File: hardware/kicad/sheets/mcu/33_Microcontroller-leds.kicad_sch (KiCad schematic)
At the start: 17 parts, among them U200 WS2815F, U201 WS2815F, U202 WS2815F, U203 WS2815F, U204 74AHCT1G125GW,125-JSM, U205 WS2815F, U206 74AHCT1G125GW,125-JSM, U207 ZX-VH3.96-4PWZ

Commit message: reorganized
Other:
- title: Microcontroller-leds -> Status LEDs
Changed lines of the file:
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@@
 	(paper "User" 297 210)
 	(title_block
-		(title "Microcontroller-leds")
+		(title "Status LEDs")
 		(date "2026-02-16")
 	)

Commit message: before final cleanup
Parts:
- renumbered C296 to C49, C295 to C50, C294 to C51, C299 to C52, C298 to C53, C297 to C54, H5 to H3, R524 to R111, R525 to R112, U204 to U27, U205 to U28, U206 to U29, U203 to U30, U202 to U31, U207 to U32, U201 to U33, U200 to U34

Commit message: pre kicad footprints
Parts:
- H3: footprint 5v rail sm-easyedapro:HDR-TH_2P-P2.54-V-M -> Connector_PinHeader_2.54mm:PinHeader_1x02_P2.54mm_Vertical
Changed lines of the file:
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@@
 			)
 		)
-		(property "Footprint" "5v rail sm-easyedapro:HDR-TH_2P-P2.54-V-M"
+		(property "Footprint" "Connector_PinHeader_2.54mm:PinHeader_1x02_P2.54mm_Vertical"
 			(at 181.61 120.65 0)
 			(effects

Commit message: imrpved footprints
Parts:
- U32: footprint 5v rail sm-easyedapro:CONN-TH_ZX-VH3.96-4PWZ -> Connector_JST:JST_VH_B4P-VH_1x04_P3.96mm_Vertical
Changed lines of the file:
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@@
 			)
 		)
-		(property "Footprint" "5v rail sm-easyedapro:CONN-TH_ZX-VH3.96-4PWZ"
+		(property "Footprint" "Connector_JST:JST_VH_B4P-VH_1x04_P3.96mm_Vertical"
 			(at 196.85 133.35 0)
 			(effects

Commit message: added better footprints and steps
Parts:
- removed U32: ZX-VH3.96-4PWZ, Connector_JST:JST_VH_B4P-VH_1x04_P3.96mm_Vertical, symbol 5v rail sm-easyedapro:ZX-VH3.96-4PWZ
- added U69: VH3_96-4P_ZZ, JLCImport:VH3_96-4P_ZZ, symbol JLCImport:VH3_96-4P_ZZ
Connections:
- net +12V: now also U69.1
- net GND: now also U69.4
- net at H3.2, R112.2: now also U69.2
- net at H3.1: now also U69.3
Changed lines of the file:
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@@
-	)
-	(symbol
-		(lib_id "5v rail sm-easyedapro:ZX-VH3.96-4PWZ")
-		(at 196.85 133.35 0)
-		(unit 1)
-		(exclude_from_sim no)
-		(in_bom yes)
-		(on_board yes)
-		(dnp no)
-		(property "Reference" "U32"
-			(at 194.31 127 0)
-			(effects
-				(font
-					(size 1.27 1.27)
-				)
-				(justify left bottom)
-			)
-		)
-		(property "Value" "ZX-VH3.96-4PWZ"
-			(at 194.31 142.24 0)
-			(effects
-				(font
-					(size 1.27 1.27)
-				)
-				(justify left bottom)
-			)
-		)
-		(property "Footprint" "Connector_JST:JST_VH_B4P-VH_1x04_P3.96mm_Vertical"
-			(at 196.85 133.35 0)
-			(effects
-				(font
-					(size 1.27 1.27)
-				)
-				(hide yes)
-			)
-		)
-		(property "Datasheet" "https://item.szlcsc.com/datasheet/ZX-VH3.96-4PWZ/8427586.html"
-			(at 196.85 133.35 0)
-			(effects
-				(font
-					(size 1.27 1.27)
-				)
-				(hide yes)
-			)
-		)
-		(property "Description" "Pins Structure:1x4P Pitch:3.96mm Mounting Type:Right Angle Reference Series:VH Number of Pins:4P Number of Rows:1 Number of PINs Per Row:4 Row Spacing:- Current Rating:3A Contact Material:Brass Contact Plating:Tin Operating Temperature:-25°C~+85°C Operating"
-			(at 196.85 133.35 0)
-			(effects
-				(font
-					(size 1.27 1.27)
-				)
-				(hide yes)
-			)
-		)
-		(property "Manufacturer Part" "ZX-VH3.96-4PWZ"
-			(at 196.85 133.35 0)
-			(effects
-				(font
-					(size 1.27 1.27)
-				)
-				(hide yes)
-			)
-		)
-		(property "Manufacturer" "Megastar(兆星)"
-			(at 196.85 133.35 0)
-			(effects
-				(font
-					(size 1.27 1.27)
-				)
-				(hide yes)
-			)
-		)
-		(property "Supplier Part" "C7429669"
-			(at 196.85 133.35 0)
-			(effects
-				(font
-					(size 1.27 1.27)
-				)
-				(hide yes)
-			)
-		)
-		(property "Supplier" "LCSC"
-			(at 196.85 133.35 0)
-			(effects
-				(font
-					(size 1.27 1.27)
-				)
-				(hide yes)
-			)
-		)
-		(property "LCSC Part Name" "1x4P 间距:3.96mm 弯插 系列:VH"
-			(at 196.85 133.35 0)
-			(effects
-				(font
-					(size 1.27 1.27)
-				)
-				(hide yes)
-			)
-		)
-		(pin "2"
-		)
-		(pin "1"
-		)
-		(pin "3"
-		)
-		(pin "4"
-		)
-		(instances
-			(project "svea_powerboard_rev3"
-				(path "/3f85abf4-0b95-4c4a-b7e9-06f59ca1ea3d/5c2e021f-c2d4-49e2-8c36-9a64f1f12004/8d05c3b8-20a4-4a7f-9b20-01f8d5d5be46"
-					(reference "U32")
-					(unit 1)
-				)
-			)
-		)
 	)
 	(symbol
@@
 					(unit 1)
 				)
+			)
+		)
+	)
+	(symbol
+		(lib_id "JLCImport:VH3_96-4P_ZZ")
+		(at 194.31 134.62 0)
+		(unit 1)
+		(exclude_from_sim no)
+		(in_bom yes)
+		(on_board yes)
+		(dnp no)
+		(fields_autoplaced yes)
+		(property "Reference" "U69"
+			(at 200.66 132.0799 0)
+			(effects
+				(font
+					(size 1.27 1.27)
+				)
+				(justify left)
+			)
+		)
+		(property "Value" "VH3_96-4P_ZZ"
+			(at 200.66 134.6199 0)
+			(effects
+				(font
+					(size 1.27 1.27)
+				)
+				(justify left)
+			)
+		)
+		(property "Footprint" "JLCImport:VH3_96-4P_ZZ"
+			(at 194.31 134.62 0)
+			(effects
+				(font
+					(size 1.27 1.27)
+				)
+				(hide yes)
+			)
+		)
+		(property "Datasheet" "https://atta.szlcsc.com/upload/public/pdf/source/20230630/DF786FC43E612B301379FAB1A9219773.pdf"
+			(at 194.31 134.62 0)
+			(effects
+				(font
+					(size 1.27 1.27)
+				)
+				(hide yes)
+			)
+		)
+		(property "Description" ""
+			(at 194.31 134.62 0)
+			(effects
+				(font
+					(size 1.27 1.27)
+				)
+				(hide yes)
+			)
+		)
+		(property "LCSC" "C5379870"
+			(at 194.31 134.62 0)
+			(effects
+				(font
+					(size 1.27 1.27)
+				)
+				(hide yes)
+			)
+		)
+		(property "Manufacturer" "SHOU HAN(首韩)"
+			(at 194.31 134.62 0)
+			(effects
+				(font
+					(size 1.27 1.27)
+				)
+				(hide yes)
+			)
+		)
+		(property "Manufacturer Part" "VH3.96-4P ZZ"
+			(at 194.31 134.62 0)
+			(effects
+				(font
+					(size 1.27 1.27)
+				)
+				(hide yes)
+			)
+		)
+		(pin "2"
+		)
+		(pin "1"
+		)
+		(pin "4"
+		)
+		(pin "3"
+		)
+		(instances
+			(project ""
+				(path "/3f85abf4-0b95-4c4a-b7e9-06f59ca1ea3d/5c2e021f-c2d4-49e2-8c36-9a64f1f12004/8d05c3b8-20a4-4a7f-9b20-01f8d5d5be46"
+					(reference "U69")
+					(unit 1)
+				)

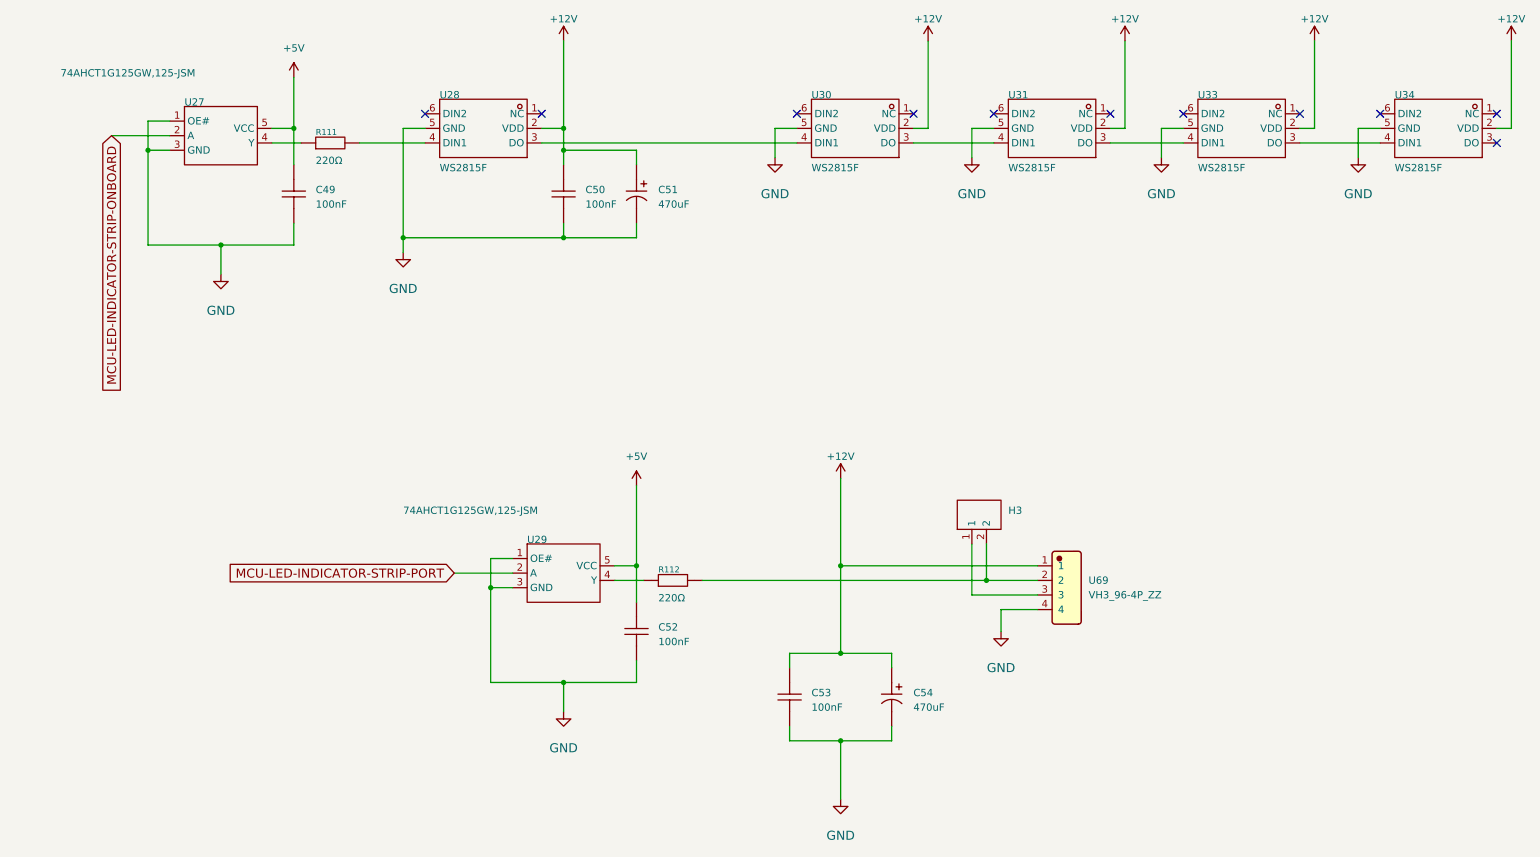
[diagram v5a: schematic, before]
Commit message: better sheet nesting for power rails
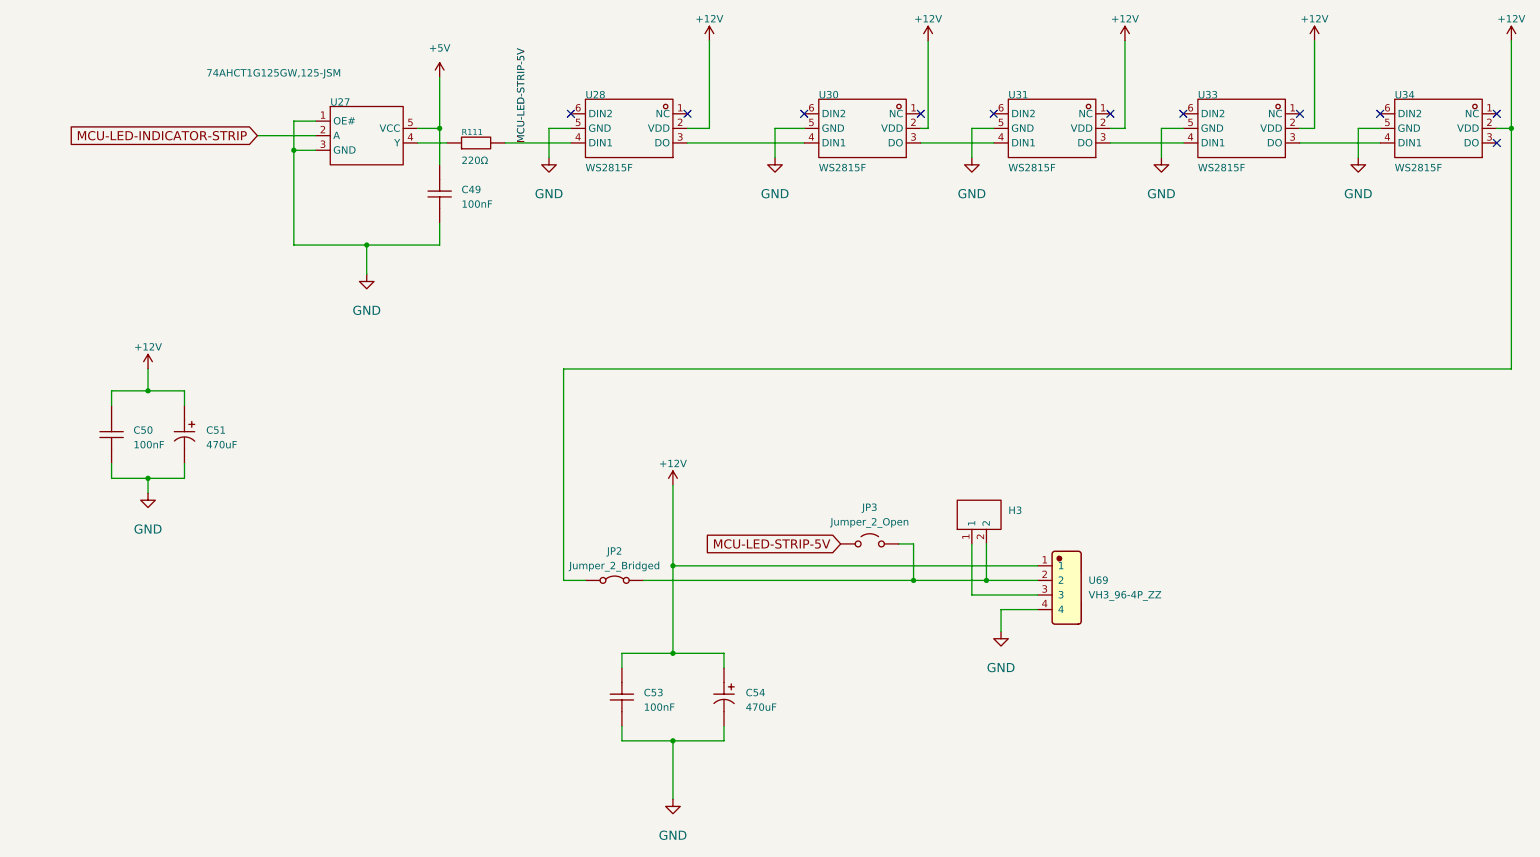
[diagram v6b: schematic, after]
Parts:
- removed C52: 100nF, Capacitor_SMD:C_0603_1608Metric, symbol 5v rail sm-easyedapro:CC0603KRX7R9BB104
- removed R112: 220Ω, Resistor_SMD:R_0603_1608Metric, symbol 5v rail sm-easyedapro:0603WAF2200T5E
- removed U29: 74AHCT1G125GW,125-JSM, Package_TO_SOT_SMD:SOT-353_SC-70-5, symbol 5v rail sm-easyedapro:74AHCT1G125GW,125-JSM
- added JP2: Jumper_2_Bridged, symbol Jumper:Jumper_2_Bridged
- added JP3: Jumper_2_Open, symbol Jumper:Jumper_2_Open
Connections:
- net +12V: now also JP2.1 (A)
- net GND: now also C51.2
- net at H3.2, U69.2: now also JP2.2 (B), JP3.2 (B)
- net MCU-LED-STRIP-5V: now reaches R111.2, U28.4 (DIN1)
- net MCU-LED-STRIP-5V: now also JP3.1 (A)
- net MCU-LED-INDICATOR-STRIP-ONBOARD renamed MCU-LED-INDICATOR-STRIP
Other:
- moved on the sheet: C49, C50, C51, C53, C54, R111, U27, U28, U30

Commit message: resheeted bms and fixed links for the 12v buck
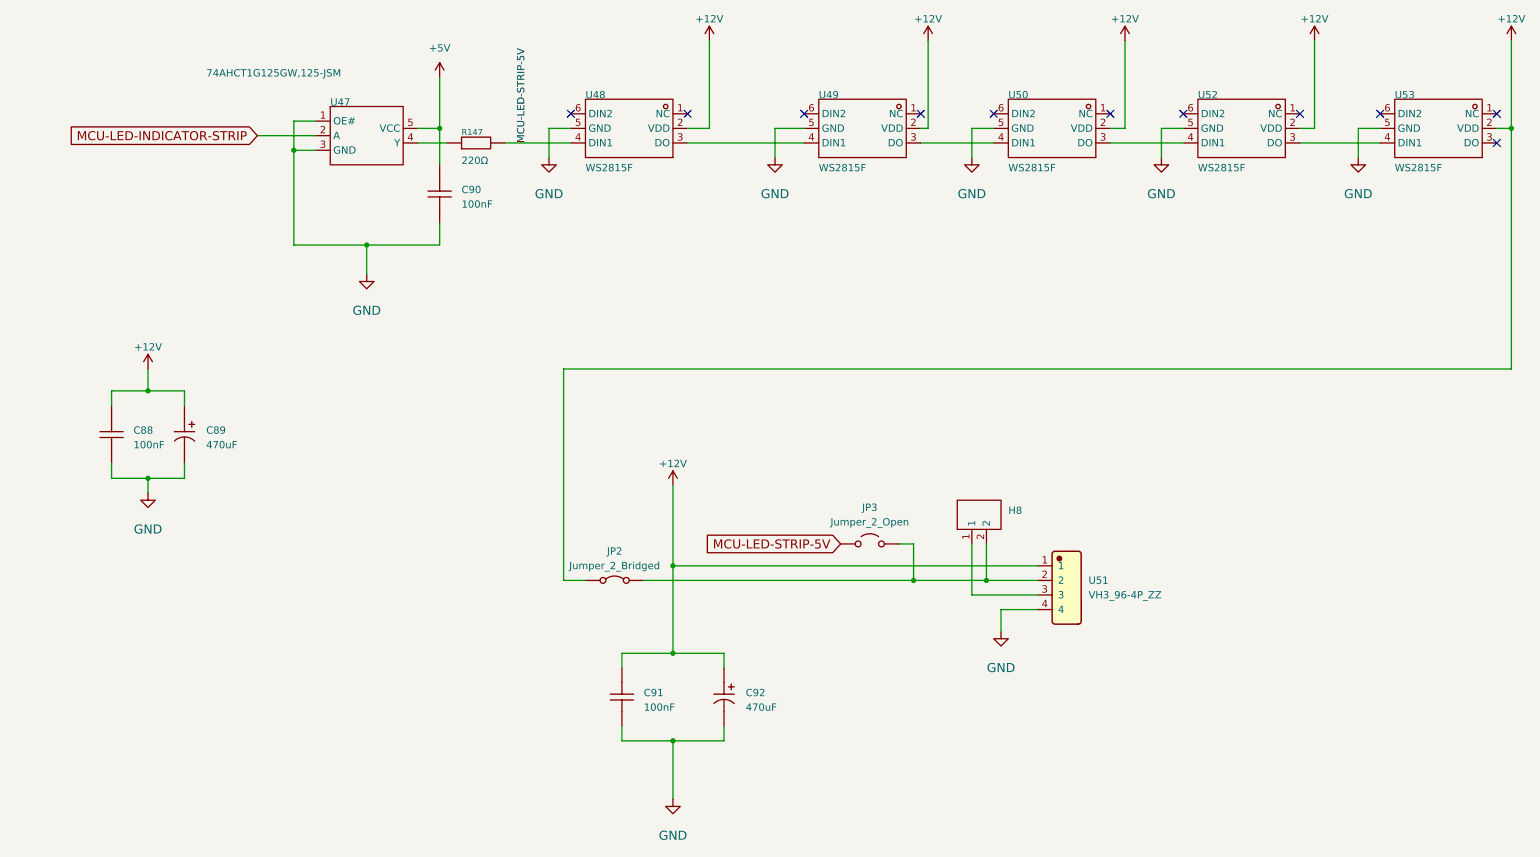
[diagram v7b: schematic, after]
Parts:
- renumbered C50 to C88, C51 to C89, C49 to C90, C53 to C91, C54 to C92, H3 to H8, R111 to R147, U27 to U47, U28 to U48, U30 to U49, U31 to U50, U69 to U51, U33 to U52, U34 to U53

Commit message: moved servos to root
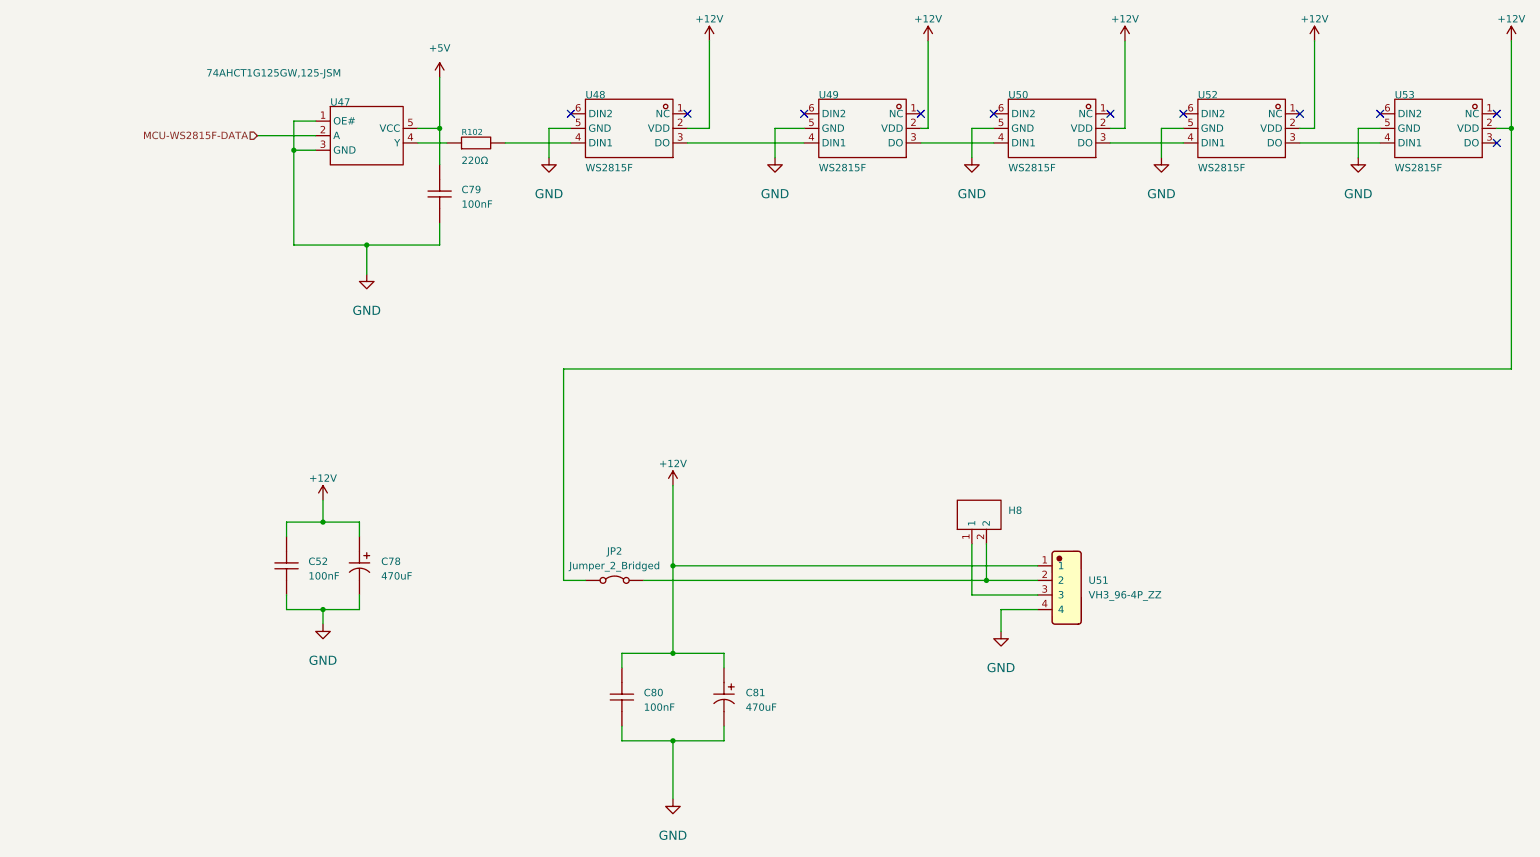
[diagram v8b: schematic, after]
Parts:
- removed JP3: Jumper_2_Open, symbol Jumper:Jumper_2_Open
- renumbered C88 to C52, C89 to C78, C90 to C79, C91 to C80, C92 to C81, R147 to R102
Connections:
- net MCU-LED-INDICATOR-STRIP renamed MCU-WS2815F-DATA
- net MCU-LED-STRIP-5V: no longer names the net of R102.2, U48.4 (DIN1)
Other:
- moved on the sheet: C52, C78
